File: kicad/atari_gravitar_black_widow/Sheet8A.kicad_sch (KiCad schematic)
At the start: 89 parts, among them Q12 2N3904

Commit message: Fixed most errors
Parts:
- gave numbers to parts that had none: 1
- renumbered NOTE to B_10
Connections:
- no-connect marks 7 -> 4
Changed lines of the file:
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@@
   (junction (at 78.74 236.22) (diameter 0) (color 0 0 0 0)
   )
-  (no_connect (at 509.905 153.035))
-  (no_connect (at 509.905 146.05))
-  (no_connect (at 509.905 147.955))
   (no_connect (at 517.525 140.335))
   (no_connect (at 509.905 134.62))
@@
   (symbol (lib_id "Star_Wars_Vector_PCB:LF13201") (at 509.905 140.335 0) (unit 2)
     (in_bom yes) (on_board yes)
-    (property "Reference" "NOTE" (id 0) (at 509.905 143.51 0))
+    (property "Reference" "B_10" (id 0) (at 509.905 143.51 0))
     (property "Value" "LF13201" (id 1) (at 516.89 139.065 0))
     (property "Footprint" "Star_Wars_Vector_PCB:DIP16" (id 2) (at 509.905 140.335 0)
@@
   (symbol (lib_id "Star_Wars_Vector_PCB-rescue:2N3906") (at 170.815 186.69 0) (mirror x) (unit 1)
     (in_bom yes) (on_board yes)
-    (property "Reference" "Q?" (id 0) (at 175.895 188.595 0)
-      (effects (font (size 1.27 1.27)) (justify left))
-    )
+    (property "Reference" "Q11" (id 0) (at 175.895 188.595 0)
+      (effects (font (size 1.27 1.27)) (justify left))
+    )

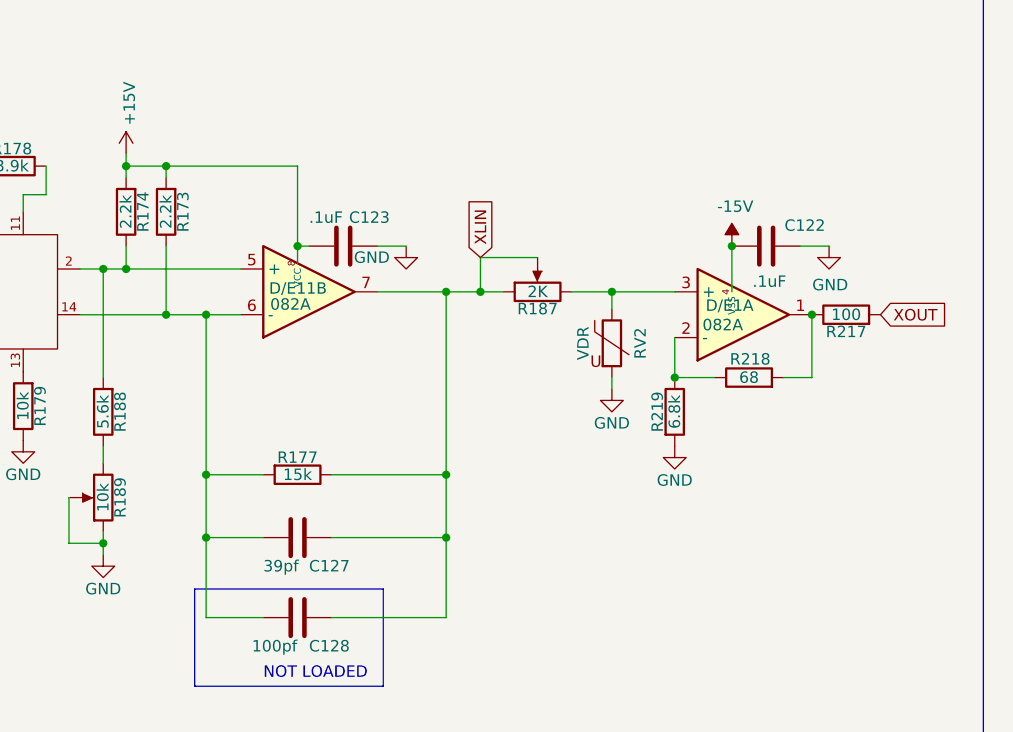
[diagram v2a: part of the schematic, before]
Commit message: Worked on removing the warnings
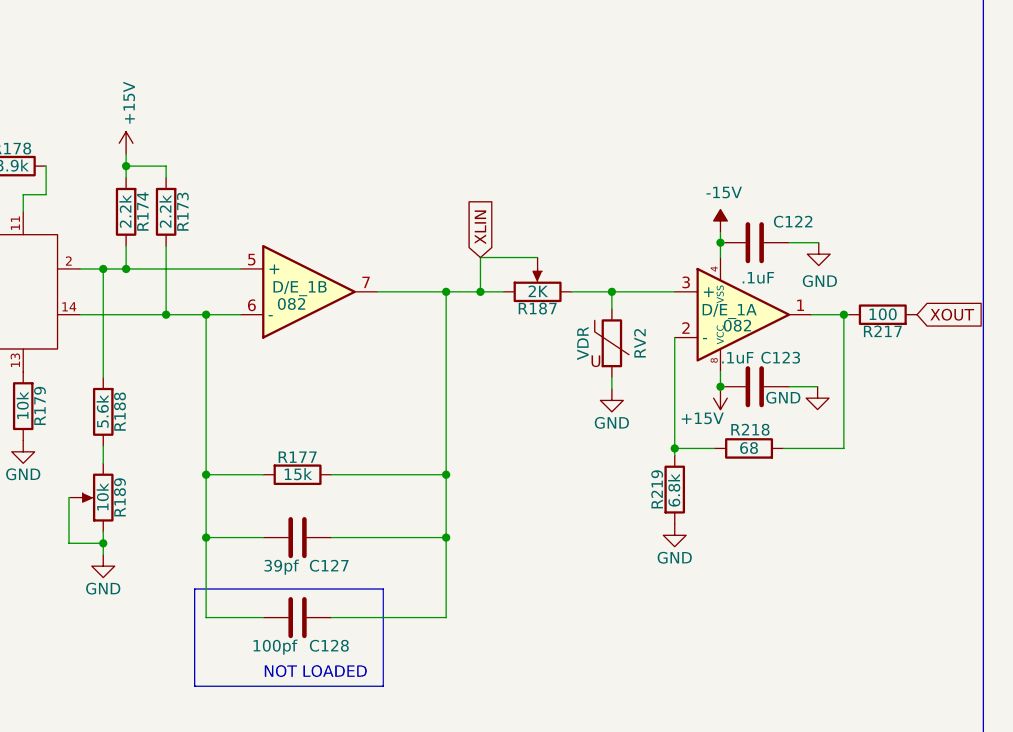
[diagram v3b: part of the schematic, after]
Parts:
- removed D/E1, D/E11: 082A, symbol atari_grav_bw:082A
- added D/E_1: 082, symbol atari_grav_bw:082
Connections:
- net +15V: now also D/E_1.8 (VCC)
- net -15V: now also D/E_1.4 (VSS)
- net XLIN: now also D/E_1.7
- net at R187.3, RV2.1: now also D/E_1.3 (+)
- net at R218.1, R219.1: now also D/E_1.2 (-)
- net at C_11.2, R174.1, R188.2: now also D/E_1.5 (+)
- net at C127.2, C128.2, C_11.14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: now also D/E_1.6 (-)
- net at R217.1, R218.2: now also D/E_1.1
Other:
- moved on the sheet: C122, C123, R217, R218, R219

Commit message: Removed more warnings - 25 warnings remain
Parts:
- removed Q12: 2N3904, quantum_arcade_pcb:GenTrans, symbol Star_Wars_Vector_PCB-rescue:2N3904
- removed R187: 2K, Star_Wars_Vector_PCB:PotBlk, symbol Star_Wars_Vector_PCB-rescue:POT
- removed R189, R192: 10k, Star_Wars_Vector_PCB:PotBlk, symbol Star_Wars_Vector_PCB-rescue:POT
- removed R98, R99: 500, Star_Wars_Vector_PCB:PotBlk, symbol Star_Wars_Vector_PCB-rescue:POT
- added Q12: 2N3904, symbol atari_grav_bw:NPN
- added R187: 2k, symbol atari_grav_bw:POT
- added R189, R192: 10k, symbol atari_grav_bw:POT
- added R98, R99: 500, symbol atari_grav_bw:POT
- A/B_11, C_11, K_9: footprint Star_Wars_Vector_PCB:DIP14 -> (none)
- A/B_9: footprint Star_Wars_Vector_PCB:DIP20 -> (none)
- A_10: footprint Star_Wars_Vector_PCB:DIP8 -> (none)
- B_10, D_9: footprint Star_Wars_Vector_PCB:DIP16 -> (none)
- C112, C113, C127, C128, C77, C85: footprint quantum_arcade_pcb:CapSmall -> (none)
- C122, C123, C124, C125, C70, C71, C73, C76, C78, C86, C87, C88, C89, R100, R101, R159, R160, R161, R162, R163, R164, R165, R166, R167, R168, R169, R170, R171, R172, R173, R174, R175, R176, R177, R178, R179, R180, R181, R182, R183, R184, R185, R186, R188, R217, R218, R219, R74, R75, R76, R77, R78, R79, R80, R81, R87, R88, R89, R90, R91, R94, R95, RV2: footprint quantum_arcade_pcb:GenComp -> (none)
- C80: footprint quantum_arcade_pcb:CapInt -> (none)
- CR4: footprint quantum_arcade_pcb:Diode -> (none)
- Q11: footprint quantum_arcade_pcb:GenTrans -> (none)
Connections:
- net GND: now also Q12.1 (E), R189.1, R189.2, R192.1, R192.2
- net XBIP: now also R99.1, R99.2
- net XLIN: now also R187.1, R187.2
- net YBIP: now also R98.1, R98.2
- net at C112.2, R159.2, R160.1: now also Q12.3 (C)
- net at R188.1: now also R189.3
- net at D/E_1.3 (+), RV2.1: now also R187.3
- net at C113.1, R161.1: now also Q12.2 (B)
- net at R183.1: now also R192.3
- net at R165.1: now also R98.3
- net at R168.1: now also R99.3

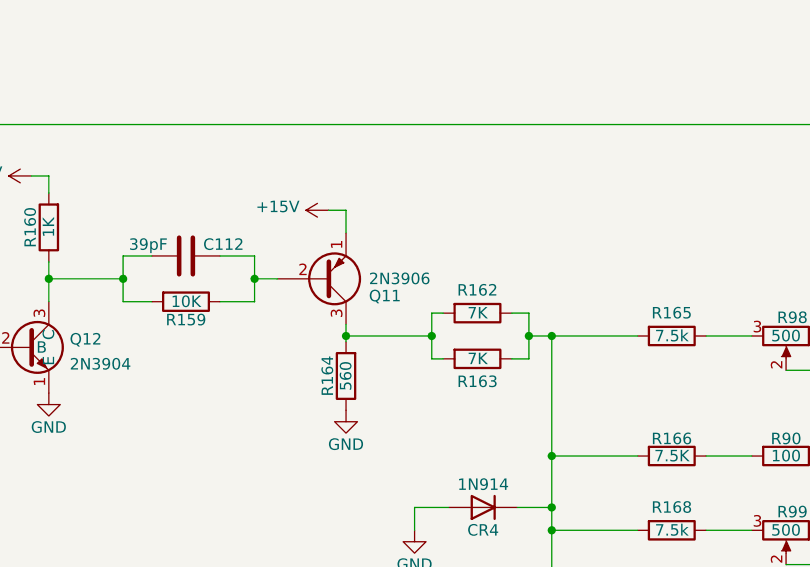
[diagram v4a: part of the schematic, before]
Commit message: 20 warnings left kicad 6.0
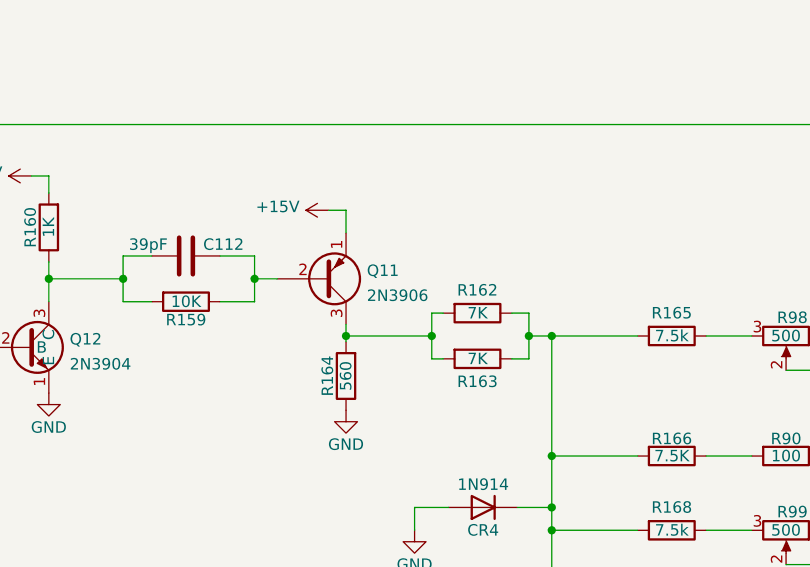
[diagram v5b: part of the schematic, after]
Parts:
- removed Q11: 2N3906, symbol Star_Wars_Vector_PCB-rescue:2N3906
- added Q11: 2N3906, Package_TO_SOT_THT:TO-92_Inline, symbol Transistor_BJT:2N3906
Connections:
- net +15V: now also Q11.1 (E)
- net at C112.1, R159.1: now also Q11.2 (B)
- net at R162.2, R163.2, R164.2: now also Q11.3 (C)
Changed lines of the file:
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@@
     (pin "2")
+  )
+  (symbol (lib_id "Transistor_BJT:2N3906") (at 170.815 186.69 0) (mirror x) (unit 1)
+    (in_bom yes) (on_board yes) (fields_autoplaced)
+    (property "Reference" "Q11" (id 0) (at 175.6664 185.7815 0)
+      (effects (font (size 1.27 1.27)) (justify left))
+    )
+    (property "Value" "2N3906" (id 1) (at 175.6664 188.5566 0)
+      (effects (font (size 1.27 1.27)) (justify left))
+    )
+    (property "Footprint" "Package_TO_SOT_THT:TO-92_Inline" (id 2) (at 175.895 184.785 0)
+      (effects (font (size 1.27 1.27) italic) (justify left) hide)
+    )
+    (property "Datasheet" "https://www.onsemi.com/pub/Collateral/2N3906-D.PDF" (id 3) (at 170.815 186.69 0)
+      (effects (font (size 1.27 1.27)) (justify left) hide)
+    )
+    (pin "1")
+    (pin "2")
+    (pin "3")
   )
   (symbol (lib_id "quantum_arcade_pcb:MC1495LA") (at 459.105 81.915 0) (unit 1)
@@
     (pin "2")
   )
-  (symbol (lib_id "Star_Wars_Vector_PCB-rescue:2N3906") (at 170.815 186.69 0) (mirror x) (unit 1)
-    (in_bom yes) (on_board yes)
-    (property "Reference" "Q11" (id 0) (at 175.895 188.595 0)
-      (effects (font (size 1.27 1.27)) (justify left))
-    )
-    (property "Value" "2N3906" (id 1) (at 175.895 186.69 0)
-      (effects (font (size 1.27 1.27)) (justify left))
-    )
-    (property "Footprint" "" (id 2) (at 175.895 184.785 0)
-      (effects (font (size 1.27 1.27) italic) (justify left) hide)
-    )
-    (property "Datasheet" "" (id 3) (at 170.815 186.69 0)
-      (effects (font (size 1.27 1.27)) (justify left) hide)
-    )
-    (pin "1")
-    (pin "2")
-    (pin "3")
-  )
   (symbol (lib_id "power:GND") (at 554.99 92.456 0) (unit 1)

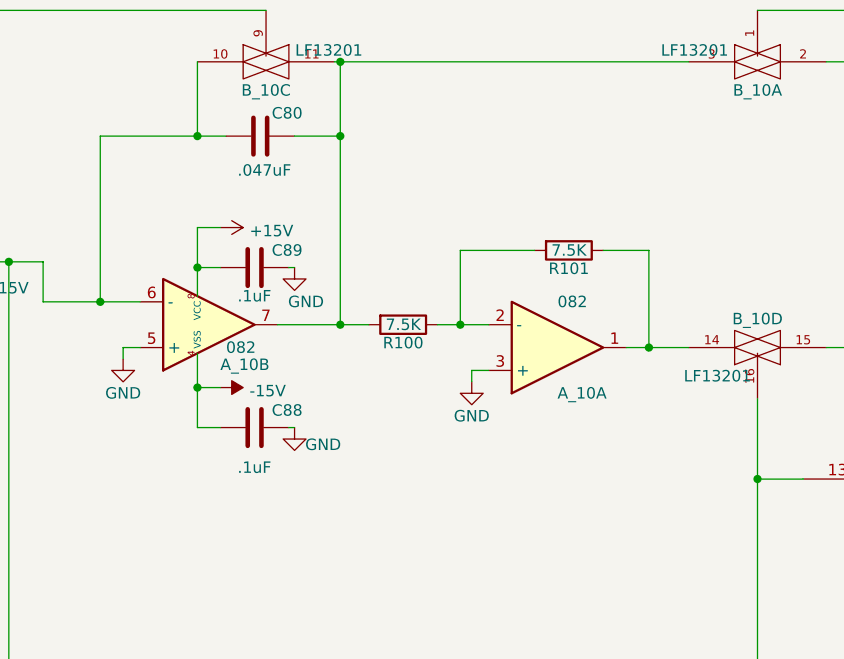
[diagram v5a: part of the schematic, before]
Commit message: Fixed all warnings and errors
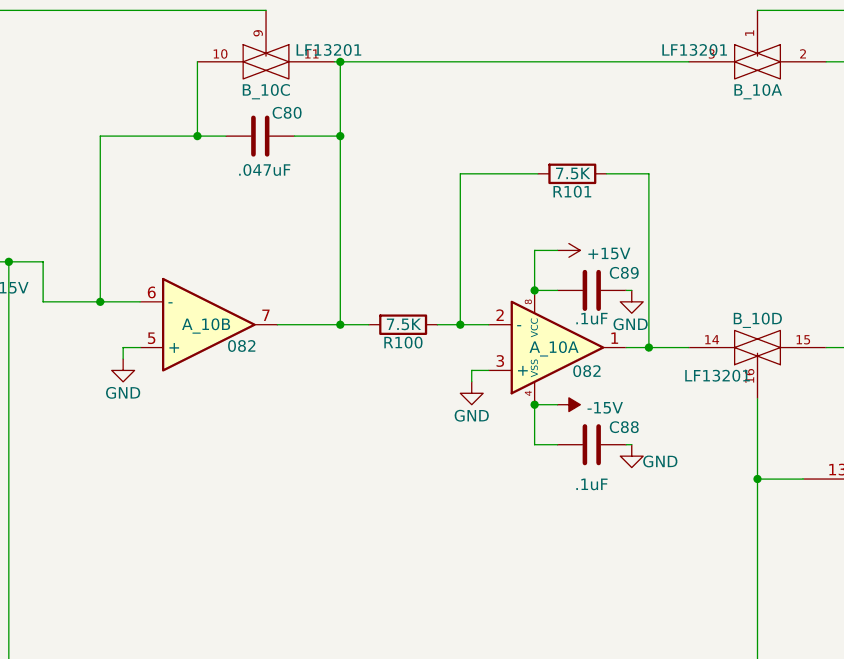
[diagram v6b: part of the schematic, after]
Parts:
- removed A_10: 082, symbol Star_Wars_Vector_PCB:082
- added A_10: 082, symbol atari_grav_bw:082
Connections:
- net +15V: now also A_10.8 (VCC)
- net -15V: now also A_10.4 (VSS)
- net GND: now also A_10.3 (+), A_10.5 (+)
- net XBIP: now also A_10.6 (-)
- net at B_10.11, B_10.3, C80.1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: now also A_10.7
- net at R100.1, R101.2: now also A_10.2 (-)
- net at B_10.14, R101.1: now also A_10.1
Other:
- moved on the sheet: C88, C89, R101

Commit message: test traces
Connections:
- net GND: no longer R91.1
- net XREF: now reaches A/B_9.14 (VR+), R94.1
- net XREF: now also R91.1
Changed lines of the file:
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@@
   (junction (at 325.755 76.2) (diameter 0) (color 0 0 0 0)
+  )
+  (junction (at 289.56 97.79) (diameter 0) (color 0 0 0 0)
   )
   (junction (at 341.63 76.2) (diameter 0) (color 0 0 0 0)
@@
     (stroke (width 0) (type default) (color 0 0 0 0))
   )
+  (wire (pts (xy 231.648 232.029) (xy 292.862 232.029))
+    (stroke (width 0) (type default) (color 0 0 0 0))
+  )
   (wire (pts (xy 341.63 67.945) (xy 380.365 67.945))
     (stroke (width 0) (type default) (color 0 0 0 0))
@@
     (stroke (width 0) (type default) (color 0 0 0 0))
   )
-  (wire (pts (xy 226.06 227.965) (xy 289.56 227.965))
-    (stroke (width 0) (type default) (color 0 0 0 0))
-  )
   (wire (pts (xy 229.235 196.85) (xy 229.235 193.04))
     (stroke (width 0) (type default) (color 0 0 0 0))
@@
     (stroke (width 0) (type default) (color 0 0 0 0))
   )
+  (wire (pts (xy 226.06 227.965) (xy 231.648 227.965))
+    (stroke (width 0) (type default) (color 0 0 0 0))
+  )
   (wire (pts (xy 426.72 149.86) (xy 424.18 149.86))
     (stroke (width 0) (type default) (color 0 0 0 0))
@@
     (stroke (width 0) (type default) (color 0 0 0 0))
   )
+  (wire (pts (xy 292.862 97.79) (xy 289.56 97.79))
+    (stroke (width 0) (type default) (color 0 0 0 0))
+  )
   (polyline (pts (xy 244.475 266.065) (xy 244.475 38.1))
     (stroke (width 0) (type default) (color 0 0 0 0))
@@
     (stroke (width 0) (type default) (color 0 0 0 0))
   )
+  (wire (pts (xy 231.648 227.965) (xy 231.648 232.029))
+    (stroke (width 0) (type default) (color 0 0 0 0))
+  )
   (wire (pts (xy 487.045 102.235) (xy 487.045 84.455))
     (stroke (width 0) (type default) (color 0 0 0 0))
@@
     (stroke (width 0) (type default) (color 0 0 0 0))
   )
+  (wire (pts (xy 292.862 232.029) (xy 292.862 97.79))
+    (stroke (width 0) (type default) (color 0 0 0 0))
+  )
   (wire (pts (xy 162.56 243.84) (xy 160.02 243.84))
     (stroke (width 0) (type default) (color 0 0 0 0))
@@
   )
   (wire (pts (xy 151.765 184.15) (xy 148.59 184.15))
-    (stroke (width 0) (type default) (color 0 0 0 0))
-  )
-  (wire (pts (xy 289.56 114.935) (xy 289.56 227.965))
     (stroke (width 0) (type default) (color 0 0 0 0))
   )
@@
     )
   )
-  (global_label "XREF" (shape input) (at 231.775 227.965 0) (fields_autoplaced)
+  (global_label "XREF" (shape input) (at 231.648 227.965 0) (fields_autoplaced)
     (effects (font (size 1.524 1.524)) (justify left))
-    (property "Intersheet References" "${INTERSHEET_REFS}" (id 0) (at -18.415 -547.37 0)
-      (effects (font (size 1.27 1.27)) hide)
-    )
+    (property "Intersheet References" "${INTERSHEET_REFS}" (id 0) (at -18.542 -547.37 0)
+      (effects (font (size 1.27 1.27)) hide)
+    )

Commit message: place ttl
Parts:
- A_10: footprint (none) -> Star_Wars_Vector_PCB:DIP8
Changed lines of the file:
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@@
     (property "Reference" "A_10" (id 0) (at 326.771 97.155 0))
     (property "Value" "082" (id 1) (at 330.708 99.568 0))
-    (property "Footprint" "" (id 2) (at 327.025 97.155 0)
+    (property "Footprint" "Star_Wars_Vector_PCB:DIP8" (id 2) (at 327.025 97.155 0)
       (effects (font (size 1.27 1.27)) hide)
     )
@@
     (property "Reference" "A_10" (id 0) (at 365.379 99.695 0))
     (property "Value" "082" (id 1) (at 369.062 102.362 0))
-    (property "Footprint" "" (id 2) (at 365.76 99.695 0)
-      (effects (font (size 1.27 1.27)) hide)
-    )
+    (property "Footprint" "Star_Wars_Vector_PCB:DIP8" (id 2) (at 365.76 99.695 0)
+      (effects (font (size 1.27 1.27)) hide)
+    )
